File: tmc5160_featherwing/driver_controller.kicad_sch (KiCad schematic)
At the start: 5 parts, among them J4 Conn_01x04_P1.5MM_Molex_Pico-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, J5 Conn_01x02_P1.5MM_Molex_Pico-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, U1 TMC5160A-WA, U11 MAX6816, X1 16MHz

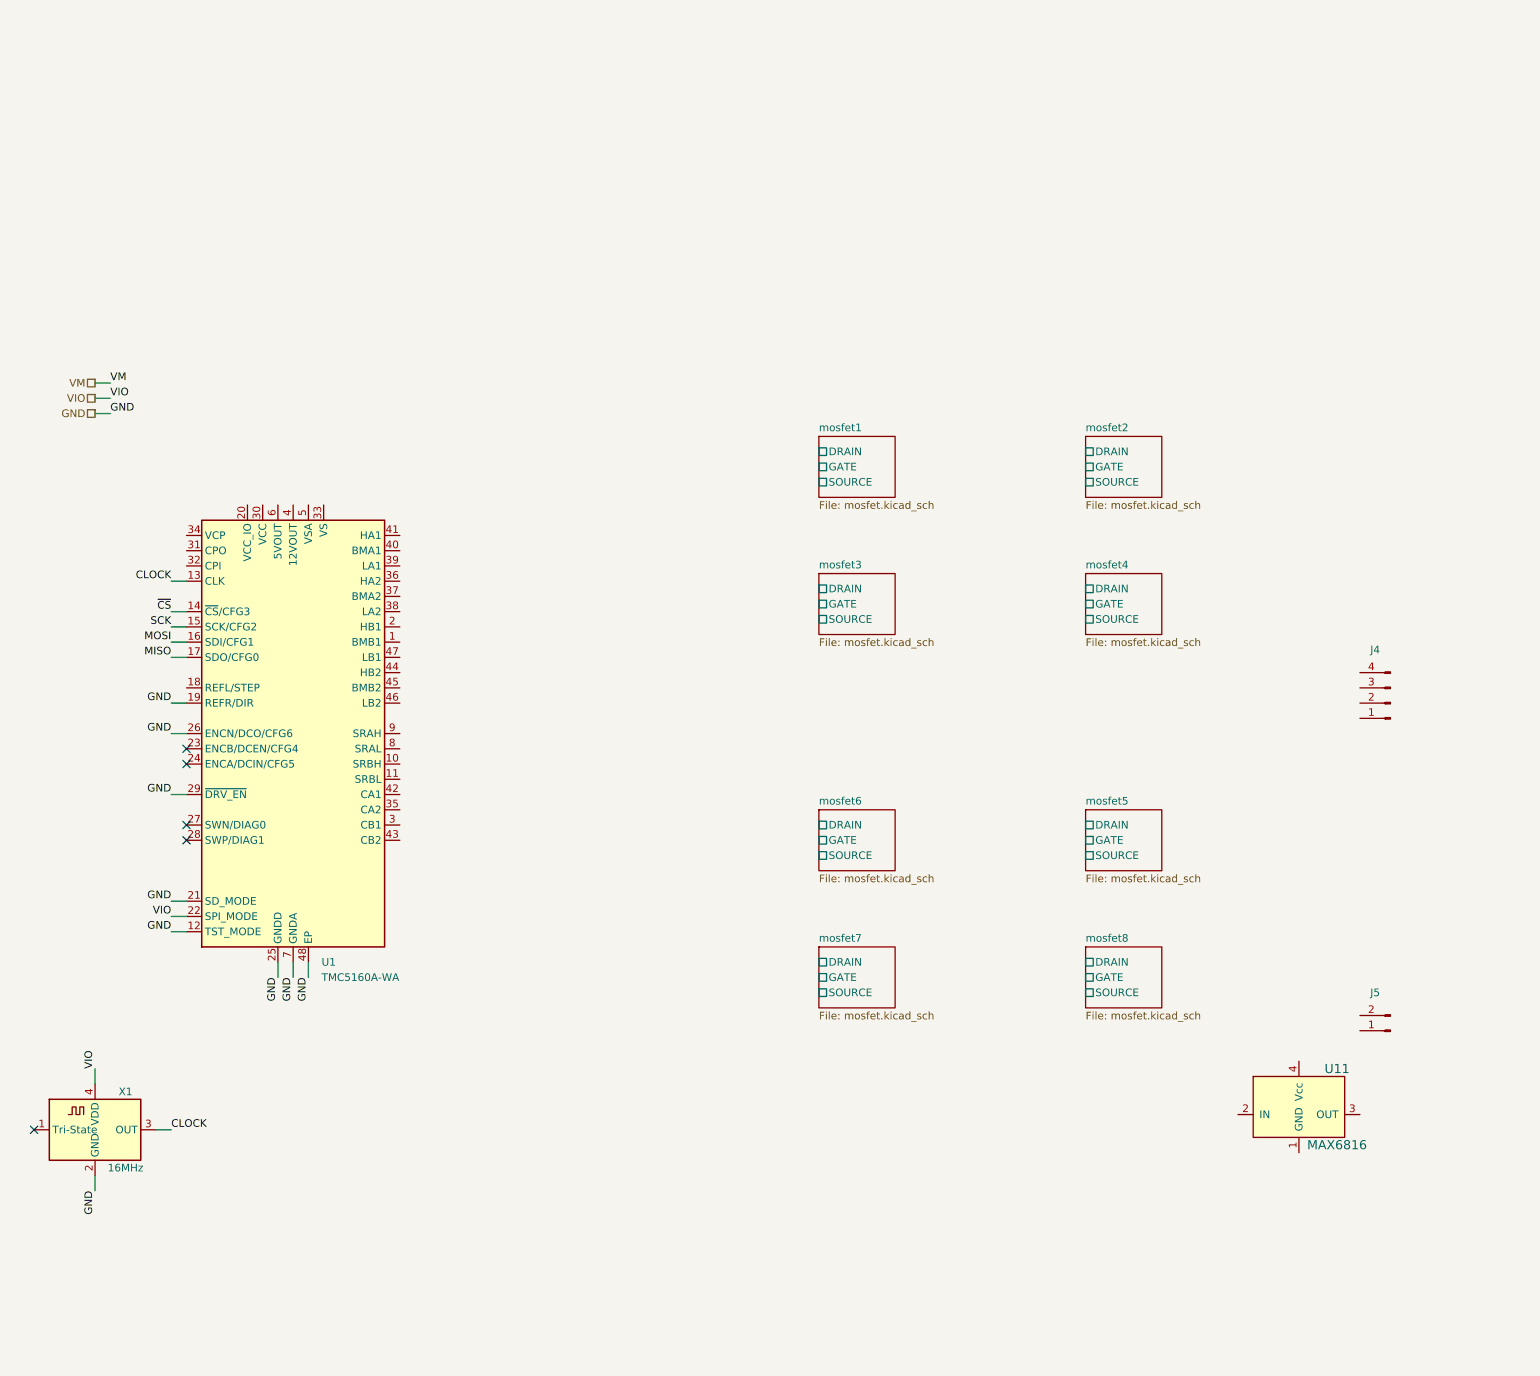
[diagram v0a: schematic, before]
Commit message: Add capactitors
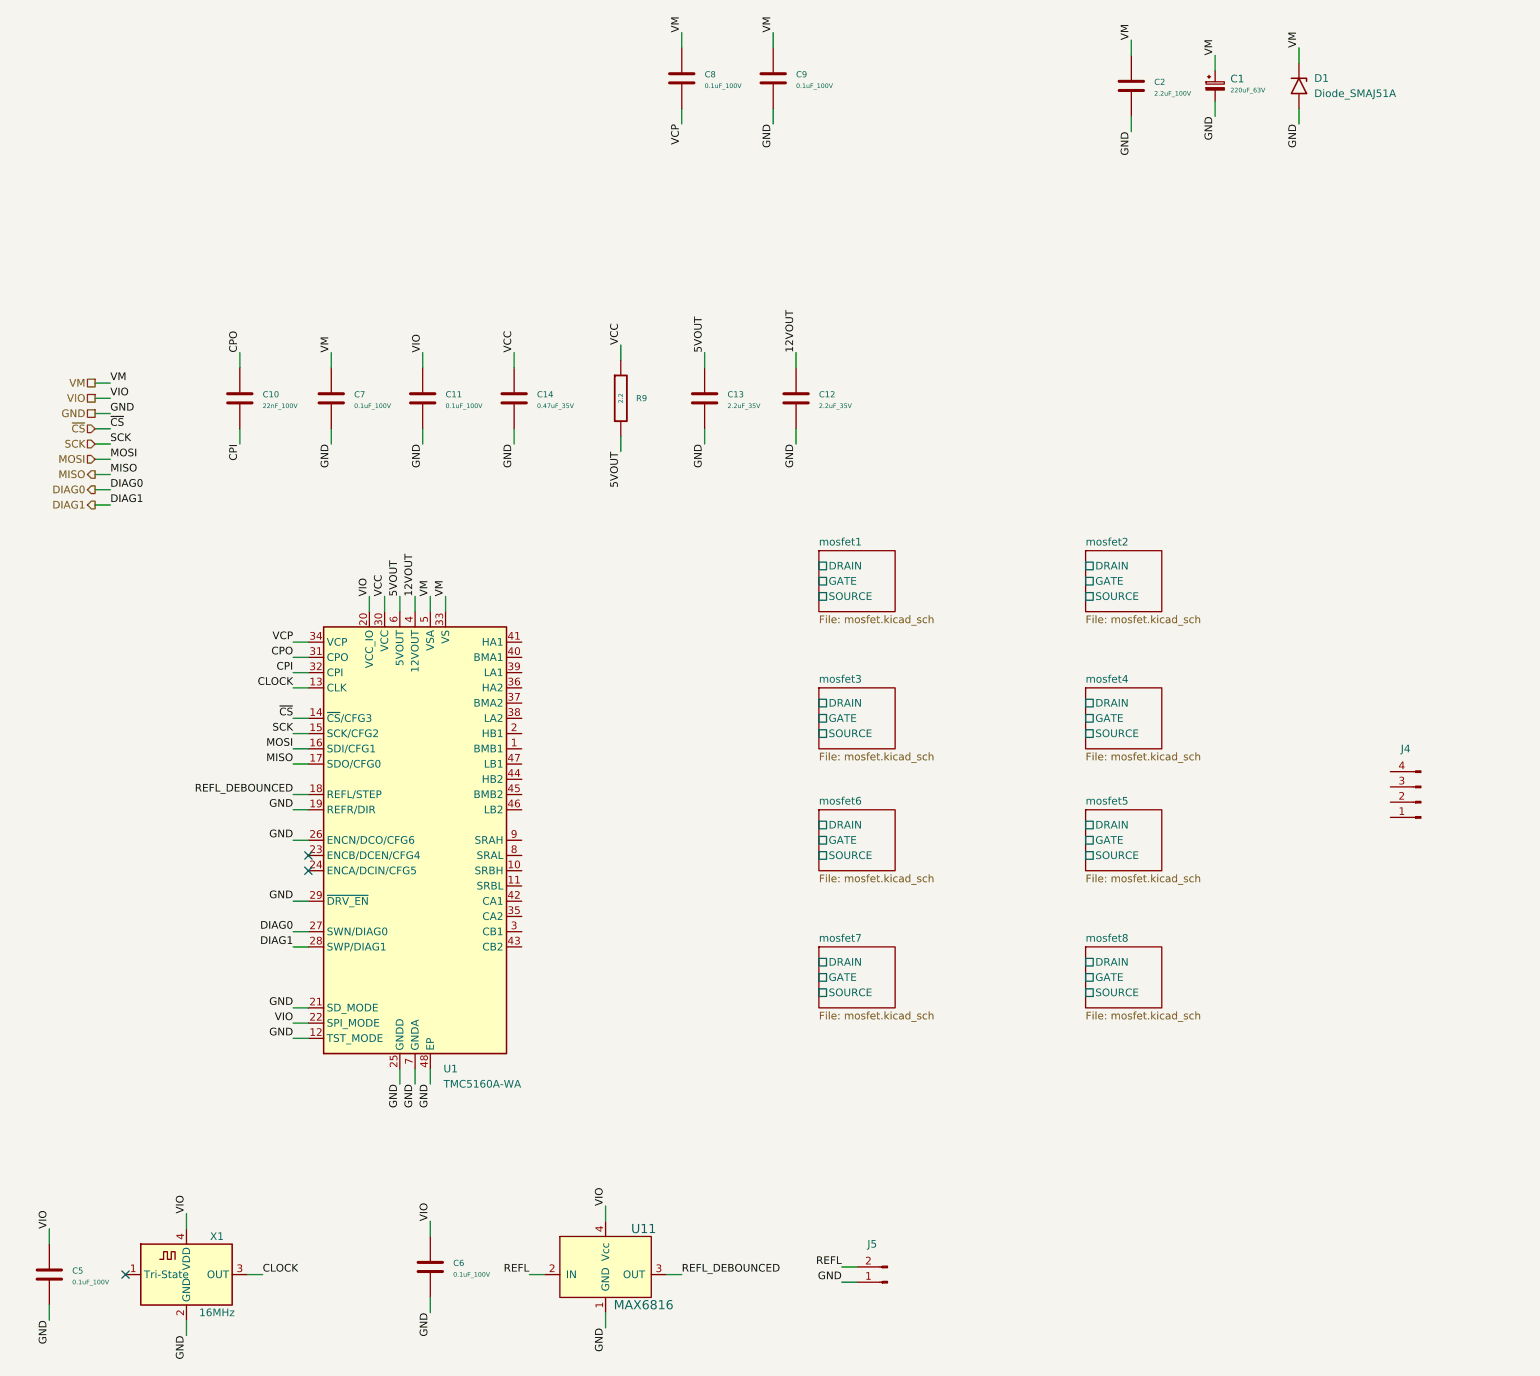
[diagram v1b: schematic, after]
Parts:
- added C1: 220uF_63V, Janelia:CP_Elec_EEEFK1J221AV, symbol Janelia:CP_220uF_63V_12.5x14.1MM
- added C10: 22nF_100V, Janelia:C_0603_1608Metric, symbol Janelia:C_22nF_100V_0603
- added C11, C5, C6, C7, C8, C9: 0.1uF_100V, Janelia:C_0402_1005Metric, symbol Janelia:C_0.1uF_100V_0402
- added C12, C13: 2.2uF_35V, Janelia:C_0402_1005Metric, symbol Janelia:C_2.2uF_35V_0402
- added C14: 0.47uF_35V, Janelia:C_0402_1005Metric, symbol Janelia:C_0.47uF_35V_0402
- added C2: 2.2uF_100V, Janelia:C_0805_2012Metric, symbol Janelia:C_2.2uF_100V_0805
- added D1: Diode_SMAJ51A, Janelia:D_SMA, symbol Janelia:Diode_SMAJ51A
- added R9: 2.2, Janelia:R_0402_1005Metric, symbol Janelia:R_2.2_0402
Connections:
- net GND: now also J5.1 (Pin_1), U11.1 (GND), C1.2, C11.2, C12.2, C13.2, C14.2, C2.2, C5.2, C6.2, C7.2, C9.2, D1.2 (A2)
- net VIO: now also U1.20 (VCC_IO), U11.4 (Vcc), C11.1, C5.1, C6.1
- net VM: now also U1.33 (VS), U1.5 (VSA), C1.1, C2.1, C7.1, C8.1, C9.1, D1.1 (A1)
- net REFL: now reaches U11.2 (IN)
- net REFL: now also J5.2 (Pin_2)
- net REFL_DEBOUNCED: now reaches U11.3 (OUT)
- net REFL_DEBOUNCED: now also U1.18 (REFL/STEP)
- net DIAG0: now reaches U1.27 (SWN/DIAG0)
- net DIAG1: now reaches U1.28 (SWP/DIAG1)
- net VCC: now reaches U1.30 (VCC)
- net VCC: now also C14.1, R9.1
- net CPO: now reaches U1.31 (CPO)
- net CPO: now also C10.1
- net CPI: now reaches U1.32 (CPI)
- net CPI: now also C10.2
- net VCP: now reaches U1.34 (VCP)
- net VCP: now also C8.2
- net 12VOUT: now reaches U1.4 (12VOUT)
- net 12VOUT: now also C12.1
- net 5VOUT: now reaches U1.6 (5VOUT)
- net 5VOUT: now also C13.1, R9.2
- no-connect marks 5 -> 3
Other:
- moved on the sheet: J4, J5, U1, U11, X1

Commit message: Add capacitors and resistors
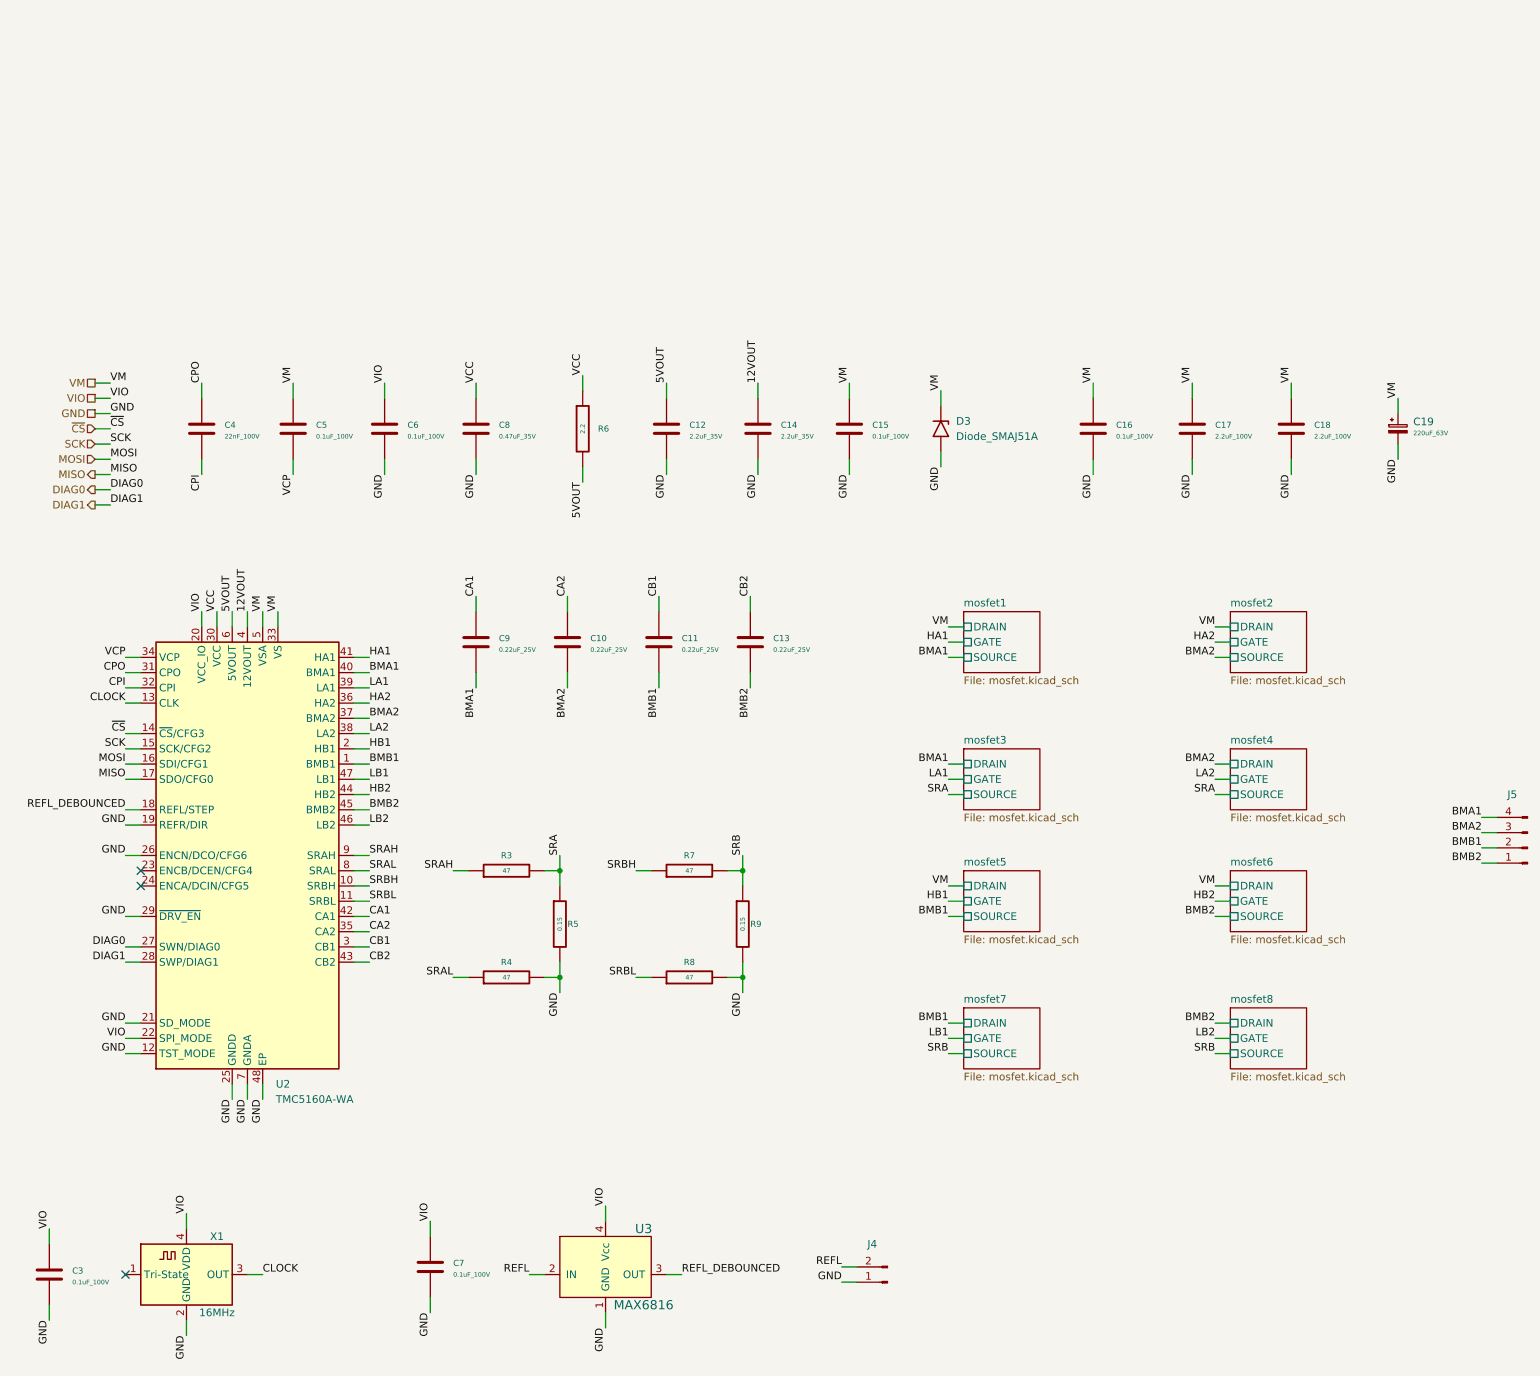
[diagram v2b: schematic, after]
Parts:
- added C10, C11, C13, C9: 0.22uF_25V, Janelia:C_0402_1005Metric, symbol Janelia:C_0.22uF_25V_0402
- added C18: 2.2uF_100V, Janelia:C_0805_2012Metric, symbol Janelia:C_2.2uF_100V_0805
- added R3, R4, R7, R8: 47, Janelia:R_0402_1005Metric, symbol Janelia:R_47_0.063W_0402
- added R5, R9: 0.15, Janelia:R_1206_3216Metric, symbol Janelia:R_0.15_1W_1206_CS
- renumbered C13 to C12, C12 to C14, C7 to C15, C9 to C16, C2 to C17, C1 to C19, C5 to C3, C10 to C4, C8 to C5, C11 to C6, C6 to C7, C14 to C8, D1 to D3, J5 to J4, J4 to J5, R9 to R6, U1 to U2, U11 to U3
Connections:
- net GND: now also C18.2, R4.2, R5.2, R8.2, R9.2
- net VM: now also C18.1
- net BMB2: now reaches J5.1 (Pin_1)
- net BMB2: now also U2.45 (BMB2), C13.2
- net BMB1: now reaches J5.2 (Pin_2)
- net BMB1: now also U2.1 (BMB1), C11.2
- net BMA2: now reaches J5.3 (Pin_3)
- net BMA2: now also U2.37 (BMA2), C10.2
- net BMA1: now reaches J5.4 (Pin_4)
- net BMA1: now also U2.40 (BMA1), C9.2
- net SRBH: now reaches U2.10 (SRBH)
- net SRBH: now also R7.1
- net SRBL: now reaches U2.11 (SRBL)
- net SRBL: now also R8.1
- net HB1: now reaches U2.2 (HB1)
- net CB1: now reaches U2.3 (CB1)
- net CB1: now also C11.1
- net CA2: now reaches U2.35 (CA2)
- net CA2: now also C10.1
- net HA2: now reaches U2.36 (HA2)
- net LA2: now reaches U2.38 (LA2)
- net LA1: now reaches U2.39 (LA1)
- net HA1: now reaches U2.41 (HA1)
- net CA1: now reaches U2.42 (CA1)
- net CA1: now also C9.1
- net CB2: now reaches U2.43 (CB2)
- net CB2: now also C13.1
- net HB2: now reaches U2.44 (HB2)
- net LB2: now reaches U2.46 (LB2)
- net LB1: now reaches U2.47 (LB1)
- net SRAL: now reaches U2.8 (SRAL)
- net SRAL: now also R4.1
- net SRAH: now reaches U2.9 (SRAH)
- net SRAH: now also R3.1
- new net SRA: R3.2, R5.1
- new net SRB: R7.2, R9.1
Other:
- moved on the sheet: C12, C14, C15, C16, C17, C19, C4, C5, C6, C8, D3, J5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
